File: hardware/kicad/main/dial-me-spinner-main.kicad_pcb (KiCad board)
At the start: 4 copper layers, 64 x 64 mm, 209 parts, among them J1 LINK, J10 SWD, J11 NFC_COIL, J20 OLED_ZIF30, J40 MOTOR, U1 RT9080-33GJ5, U10 MDBT50Q-U1MV2, U11 W25Q128JVSIQ, U12 USBLC6-2SC6, U2 TPS22917DBVR, U20 TPS61040DBVR, U21 TPS22917DBVR, U30 TMAG5273A2QDBVR, U31 LIS2DW12TR, U32 TPD4E05U06DQAR, U40 DRV8837DSGR, U41 DRV8837DSGR, U42 DRV5032FADBZR, U43 SN74LV1T34DBVR, Y1 32.768k 9pF

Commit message: WIP: firmware-rule closure / main routing in progress
Co-Authored-By: Claude Opus 5.5 <noreply@anthropic.com>
Claude-Session: https://claude.ai/code/session_01P3cqdBhxLcWY3sGUVf9LAJ
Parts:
- turned C106 to 128 degrees
- turned C132 to -37 degrees
- turned C142 to 38 degrees
- turned C144 to 53 degrees
- turned C118 to -142 degrees
- turned C120 to -127 degrees
- turned C108 to 143 degrees
- turned C130 to -52 degrees
- turned D140 to 23 degrees
- turned D146 to 68 degrees
- turned D104 to 113 degrees
- turned D134 to -22 degrees
- turned D110 to 158 degrees
- turned D128 to -67 degrees
- turned D116 to -157 degrees
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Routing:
- net VLED: track 0.00 -> 292.9 mm
- net +3V3: track 0.00 -> 213.5 mm, vias 0 -> 8
- net VSYS: track 0.00 -> 113.4 mm, vias 0 -> 2
- net I2C_SCL: track 0.00 -> 75.8 mm, vias 0 -> 3
- net CHG_INT_N: track 0.00 -> 69.5 mm, vias 0 -> 3
- net OLED_VCC_EN: track 0.00 -> 51.3 mm, vias 0 -> 2
- net I2C_SDA: track 0.00 -> 49.9 mm, vias 0 -> 3
- net MOT_B_IN1: track 0.00 -> 48.5 mm, vias 0 -> 2
- net TMAG_SDA: track 0.00 -> 47.8 mm, vias 0 -> 2
- net TMAG_SCL: track 0.00 -> 45.1 mm, vias 0 -> 3
- net /Sensors & sounder/BZ_P: track 0.00 -> 43.9 mm, vias 0 -> 2
- net /Sensors & sounder/BZ_N: track 0.00 -> 43.0 mm, vias 0 -> 2
- net HOME_N: track 0.00 -> 41.4 mm, vias 0 -> 4
- net /LED ring/LED_DIN_R: track 0.00 -> 40.5 mm, vias 0 -> 3
- net OLED_VIN: track 0.00 -> 38.5 mm, vias 0 -> 2
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
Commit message: Proportional VBAT reading margin (VBAT_est = 0.979 x reading) across tests and docs; actuator step scale 0.015 mm/step (500 steps); SPEC NFC coil, LiPo bay, ring ESD wording; fab rules per board
Full suite 729 passed, 44 strict xfails (6 accepted risks, 34 old-rule evidence, 4 'not allowed by the rule'),
0 failed; the three reading-margin rule-insufficient xfails are retired.

Co-Authored-By: Claude Opus 5.5 <noreply@anthropic.com>
Claude-Session: https://claude.ai/code/session_01P3cqdBhxLcWY3sGUVf9LAJ
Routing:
- net MOT_B_IN2: track 2.57 -> 22.6 mm
- net /Detent actuator & home sensor/MOT_A_OUT1: track 1.83 -> 16.6 mm, vias 1 -> 2
- net /Detent actuator & home sensor/MOT_A_OUT2: track 10.8 -> 18.4 mm, vias 2 -> 3
- net BTN_N: track 19.2 -> 23.2 mm, vias 3 -> 4
- net VBUS: track 16.6 -> 17.8 mm
- net VLED: track 292.9 -> 293.8 mm
- net /MCU, flash & debug/TP_SPARE1: track 0.00 -> 0.89 mm
- net +3V3: track 213.5 -> 214.3 mm
- net +13V_OLED: track 34.2 -> 35.0 mm
- net /LED ring/LED_D8: track 6.90 -> 7.57 mm
- net /Power & link/LSW_CT: track 1.79 -> 2.43 mm

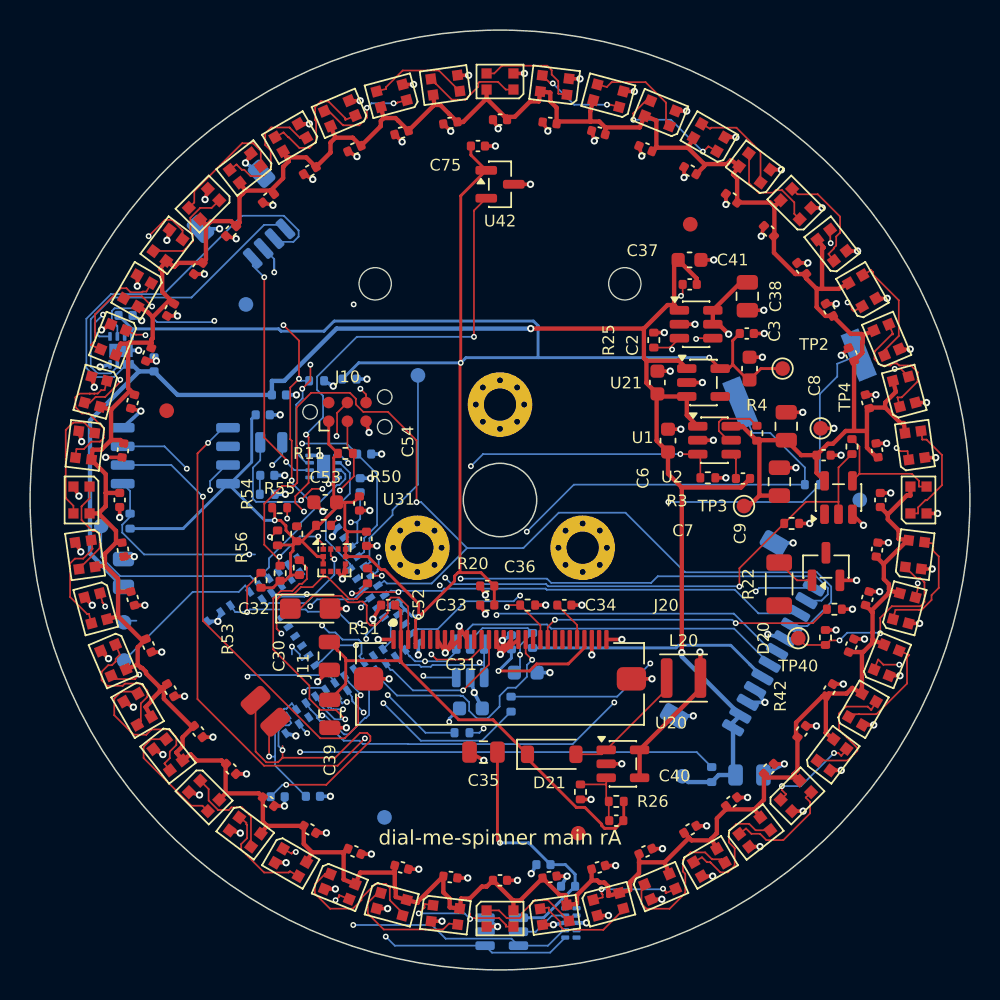
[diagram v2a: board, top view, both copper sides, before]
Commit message: Main board routed: 0 unconnected, DRC clean (no errors or warnings) with schematic parity
Freerouting (placement variant with J10 at the SWD pins) left 11 connections open; finish_route completed them.
No copper under the clamped hub flange / M4 nut or near the centre hole (65 pieces re-routed). Board title on the
bottom silk. finish_route: ends anchored like a router (tracks split at T-joints, short links to via centres),
supplies never ripped, large victim nets lose only the conflicting copper, a net's connections all route in one
round, windows sized from the smaller cluster; layout: --complete repeats until the clean-up keeps every joint,
GND fix-up falls back to a signal-size via, the dangling pruner compares against the prior unconnected count.

Co-Authored-By: Claude Opus 5.5 <noreply@anthropic.com>
Claude-Session: https://claude.ai/code/session_01P3cqdBhxLcWY3sGUVf9LAJ
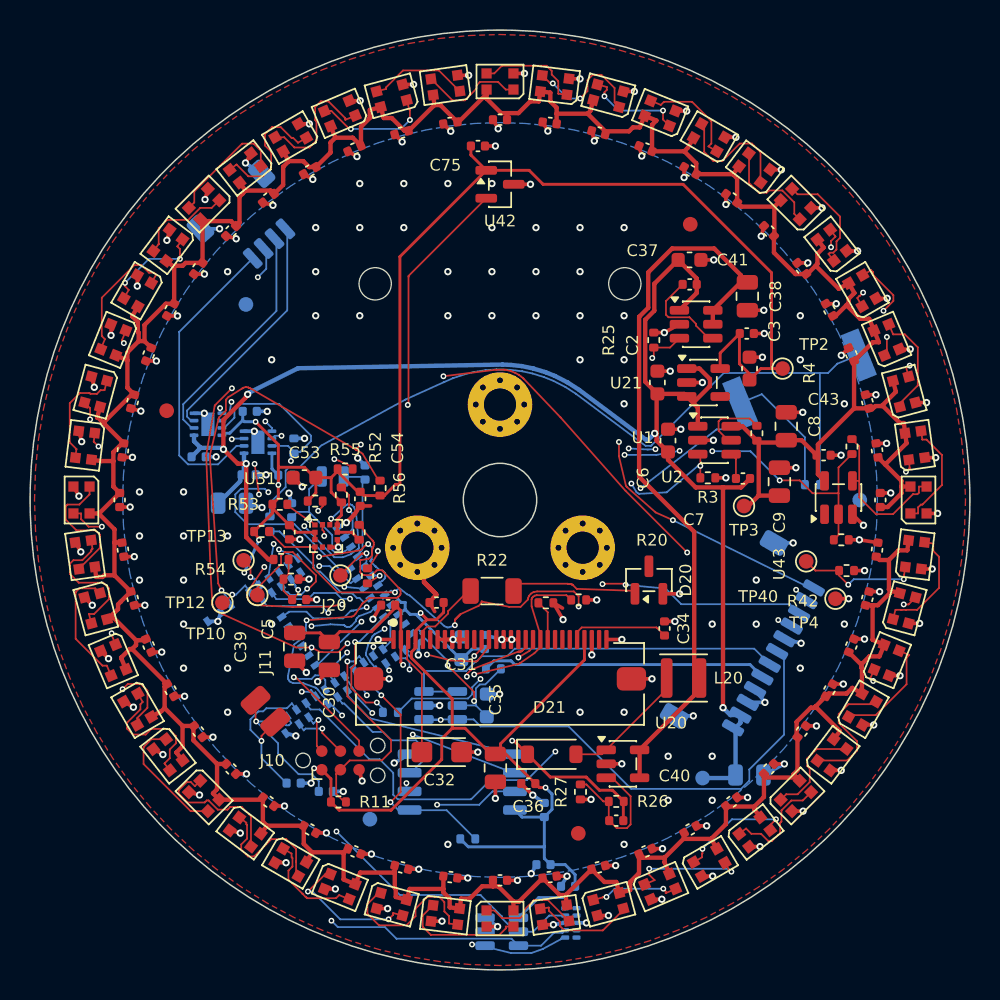
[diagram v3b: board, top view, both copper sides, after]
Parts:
- C5, R1, R2, TP10, TP11, TP12, TP13: moved to F.Cu
- moved C15 33.0 mm to (103.0, 121.1), turned to 90 degrees
- moved R1 32.8 mm to (85.1, 104.0), turned to 0 degrees
- moved R10 31.6 mm to (97.8, 123.1), turned to 0 degrees
- moved U11 29.6 mm to (97.4, 119.2)
- moved R11 23.7 mm to (89.0, 120.6)
- moved J10 23.7 mm to (89.1, 117.7)
- moved R58 20.5 mm to (84.3, 101.6)
- moved R21 19.7 mm to (103.1, 107.0)
- moved R22 19.6 mm to (99.5, 106.2), turned to 0 degrees
- moved TP11 14.6 mm to (89.1, 105.1)
- moved C36 13.7 mm to (101.9, 119.3)
- moved C32 13.3 mm to (96.0, 117.2)
- moved D20 12.1 mm to (110.1, 105.5)
- moved TP4 11.6 mm to (122.8, 106.7)
- moved C73 10.7 mm to (83.0, 94.0)
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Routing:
- net TMAG_INT_N: track 3.64 -> 45.5 mm, vias 0 -> 2
- net BTN_N: track 23.2 -> 63.8 mm
- net /MCU, flash & debug/QSPI_IO0: track 37.3 -> 11.5 mm, vias 3 -> 0
- net VSYS_SENSE: track 29.8 -> 4.85 mm
- net /MCU, flash & debug/QSPI_IO1: track 33.2 -> 8.50 mm
- net MOT_B_IN1: track 48.5 -> 24.4 mm, vias 2 -> 6
- net MOT_A_IN2: track 0.94 -> 24.0 mm, vias 1 -> 2
- net +3V3: track 214.3 -> 191.9 mm, vias 8 -> 7
- net /MCU, flash & debug/SWDCLK: track 25.6 -> 3.90 mm, vias 2 -> 1
- net I2C_SCL: track 75.8 -> 55.3 mm, vias 3 -> 6
- net /OLED display & 13 V boost/OLED_IREF: track 20.8 -> 2.76 mm, vias 2 -> 0
- net /MCU, flash & debug/QSPI_CS: track 34.2 -> 16.6 mm
- net LED_PWR_EN: track 17.7 -> 34.7 mm, vias 2 -> 3
- net /MCU, flash & debug/SWO: track 25.4 -> 10.0 mm, vias 2 -> 1
- net /MCU, flash & debug/NFC2: track 25.4 -> 11.6 mm, vias 2 -> 1
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- added copper zone on B.Cu, net GND
- added copper zone on F.Cu, net GND

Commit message: No vias on SMD or connector pads: GND fan-out, stitching and the grid router keep via rings off every SMD/connector pad (any net); --complete removes any via on a pad and re-routes. Main board re-completed (DRC clean, no warnings, parity clean; nothing on a pad), fab outputs re-released; assembly §13 #28 closed; PCB-order wording; coax comments name U12's new place
Co-Authored-By: Claude Opus 5.5 <noreply@anthropic.com>
Claude-Session: https://claude.ai/code/session_01P3cqdBhxLcWY3sGUVf9LAJ
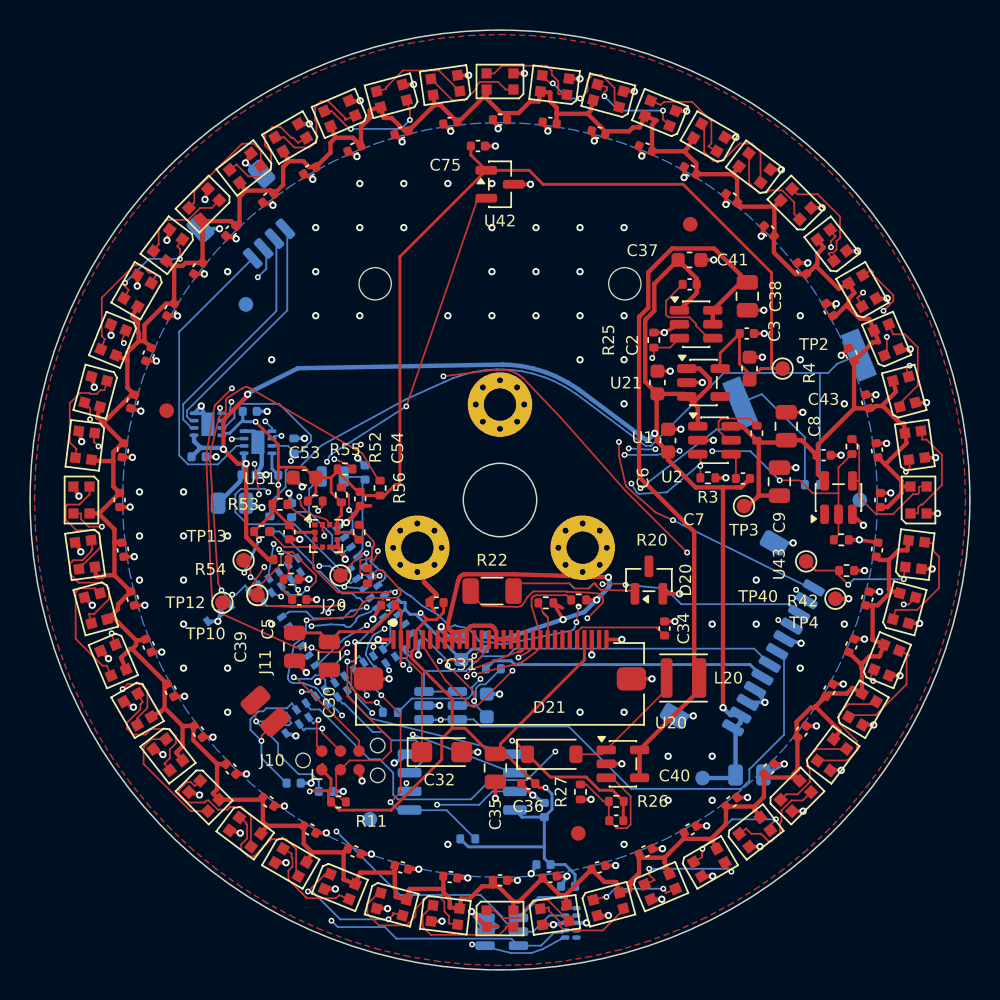
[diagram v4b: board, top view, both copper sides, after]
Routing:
- net GND: track 156.2 -> 195.1 mm, vias 221 -> 218
- net /OLED display & 13 V boost/OLED_VSL: track 5.06 -> 26.2 mm, vias 0 -> 2
- net HOME_N: track 37.4 -> 31.5 mm, vias 2 -> 3
- net IMU_INT2: track 13.3 -> 7.79 mm, vias 3 -> 2
- net +3V3: track 191.9 -> 195.1 mm
- net OLED_RES_N: track 25.5 -> 24.0 mm
- net /OLED display & 13 V boost/OLED_IREF: track 2.76 -> 1.72 mm
- net I2C_SCL: track 55.3 -> 54.8 mm, vias 6 -> 5
